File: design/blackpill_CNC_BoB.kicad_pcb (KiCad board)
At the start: 4 copper layers, 302 parts, among them J101 ALimIN, J102 ZLimIN, J103 YLimIN, J104 XLimIN, J105 CS_IN, J106 FH_IN, J107 DoorIN, J108 ResetIN, J109 ProbeIN, J110 12V Power in, J111 AuxEncIn, J112 5V Power out, J113 ADC_in_1, J114 ADC_in_2, J115 stepDriverLim, J116 Reset, J117 UART1, J118 I2C, J119 SpindleVFD, J120 Spindle/Coolant, J121 Spindle, J122 Coolant, J123 AuxOut, J124 XStepDrv, J125 YStepDrv, J126 ZStepDrv, J127 AStepDrv, J128 Driver Power in/out, J129 Relais Power in/out, U101 TLP290-4, U102 TLP290-4, U103 TLP290-4, U104 74LVC2G17, U105 LD1117S50TR_SOT223, U106 LM358, U107 TLV9001, U108 TLV9001, U109 YAAJ_WeAct_BlackPill_Part_Like, U110 TLV9001, U111 TLV9001, U112 74HCT541, U113 74HCT541, U114 74HCT541, U115 ULN2003A, U116 ULN2003A, U117 ULN2003A

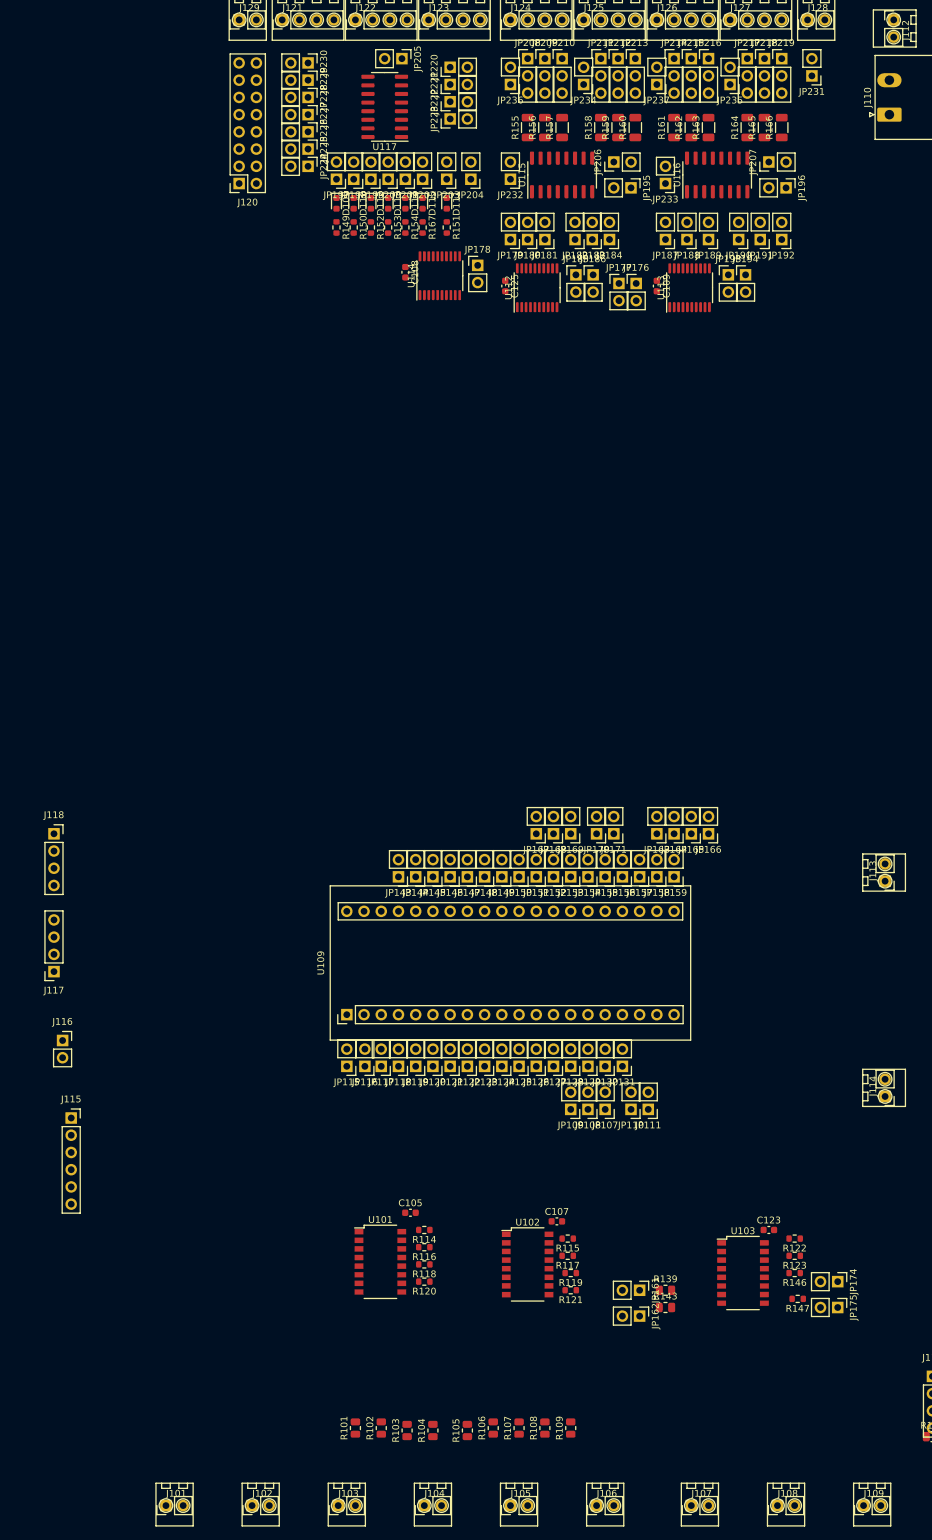
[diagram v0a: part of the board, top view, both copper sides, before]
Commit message: start placing controller
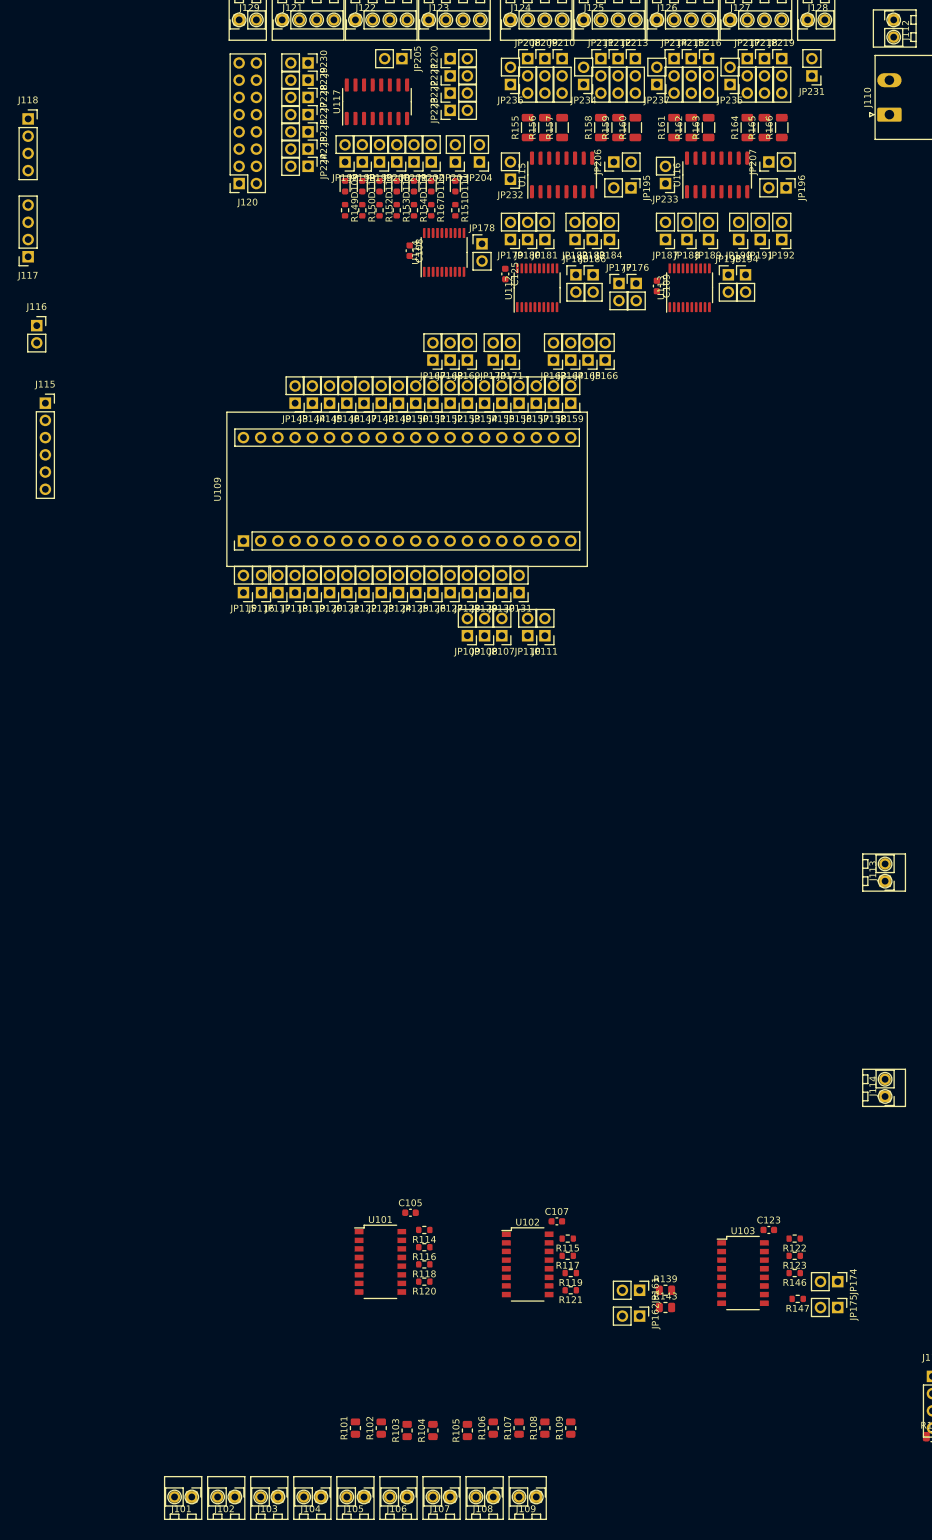
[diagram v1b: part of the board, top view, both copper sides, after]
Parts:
- moved J115 105.5 mm to (-26.7, 58.4)
- moved J117 105.5 mm to (-29.2, 36.8)
- moved J116 105.5 mm to (-27.9, 47.0)
- moved J118 105.5 mm to (-29.2, 16.5)
- moved JP107 71.5 mm to (40.6, 92.7)
- moved JP108 71.5 mm to (38.1, 92.7)
- moved JP109 71.5 mm to (35.6, 92.7)
- moved JP110 71.5 mm to (44.5, 92.7)
- moved JP111 71.5 mm to (47.0, 92.7)
- moved JP115 71.5 mm to (2.54, 86.4)
- moved JP116 71.5 mm to (5.21, 86.4)
- moved JP117 71.5 mm to (7.62, 86.4)
- moved JP118 71.5 mm to (10.2, 86.4)
- moved JP119 71.5 mm to (12.7, 86.4)
- moved JP120 71.5 mm to (15.2, 86.4)
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
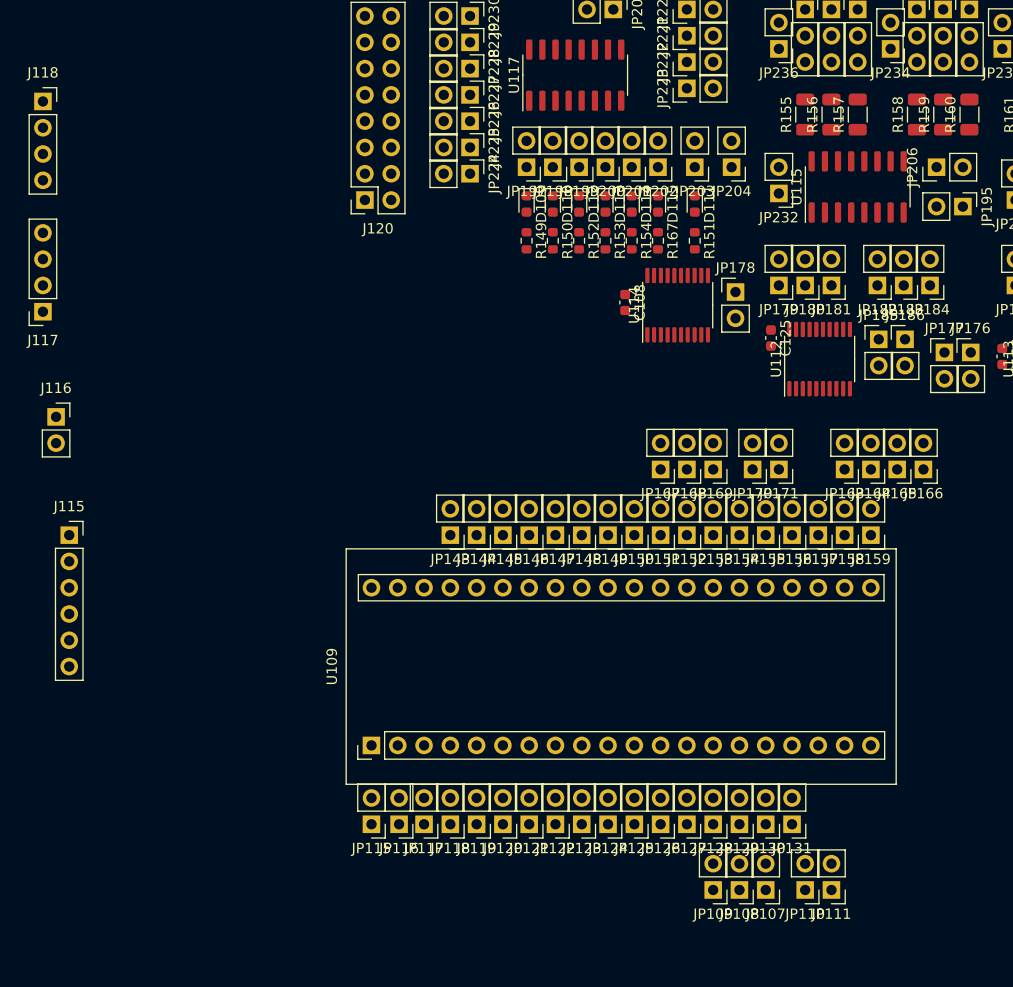
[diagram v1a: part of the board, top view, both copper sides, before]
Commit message: added exp power pins
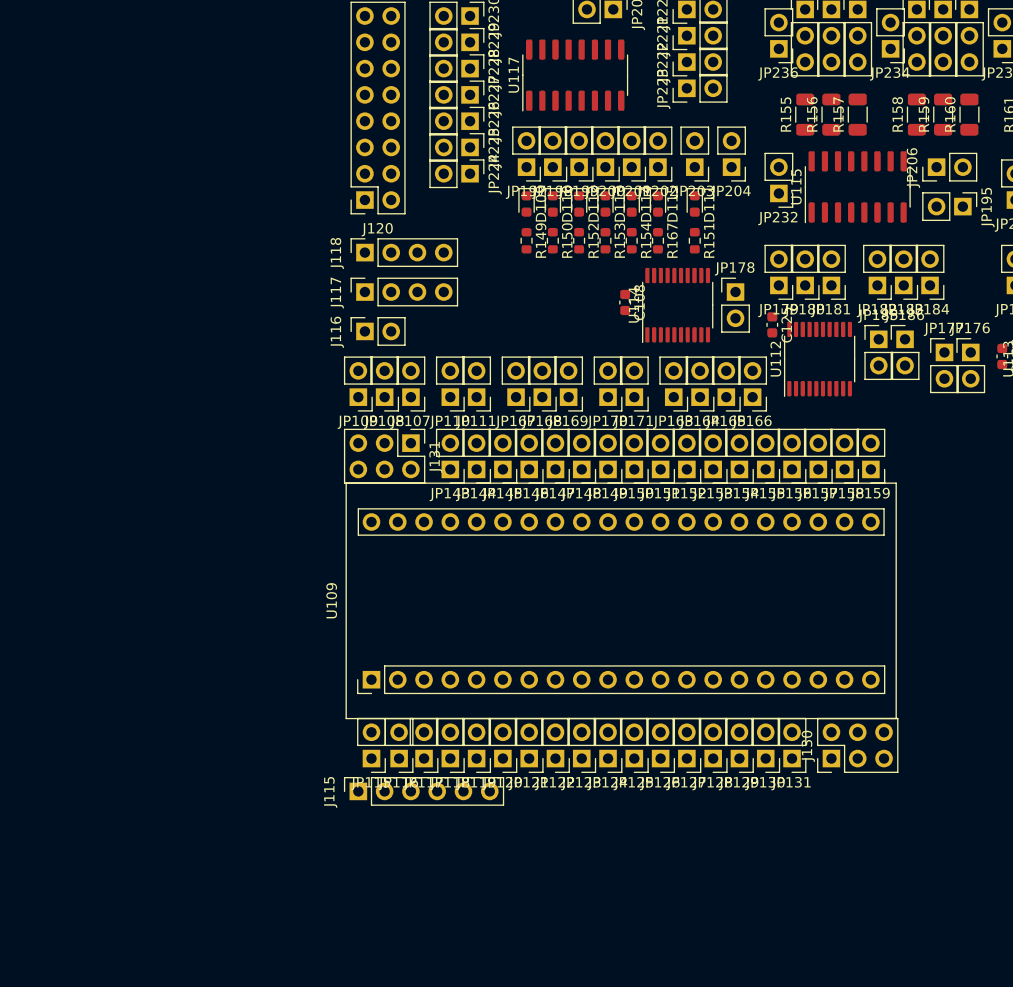
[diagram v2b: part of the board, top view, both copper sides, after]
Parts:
- added J130: Conn_02x03_Odd_Even, Connector_PinHeader_2.54mm:PinHeader_2x03_P2.54mm_Vertical, F.Cu at (47.0, 80.0)
- added J131: Conn_02x03_Odd_Even, Connector_PinHeader_2.54mm:PinHeader_2x03_P2.54mm_Vertical, F.Cu at (6.35, 49.5)
- moved JP107 58.7 mm to (6.35, 45.1)
- moved JP108 58.7 mm to (3.81, 45.1)
- moved JP109 58.7 mm to (1.27, 45.1)
- moved JP110 58.7 mm to (10.2, 45.1)
- moved JP111 58.7 mm to (12.7, 45.1)
- moved J115 37.3 mm to (1.27, 83.2), turned to 90 degrees
- moved J118 34.4 mm to (1.91, 31.1), turned to 90 degrees
- moved J117 31.2 mm to (1.91, 34.9), turned to 90 degrees
- moved J116 31.0 mm to (1.91, 38.7), turned to 90 degrees
- moved JP165 17.9 mm to (36.8, 45.1)
- moved JP166 17.9 mm to (39.4, 45.1)
- moved JP163 17.9 mm to (31.8, 45.1)
- moved JP164 17.9 mm to (34.3, 45.1)
- moved JP168 15.6 mm to (19.1, 45.1)
- moved JP169 15.6 mm to (21.6, 45.1)
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
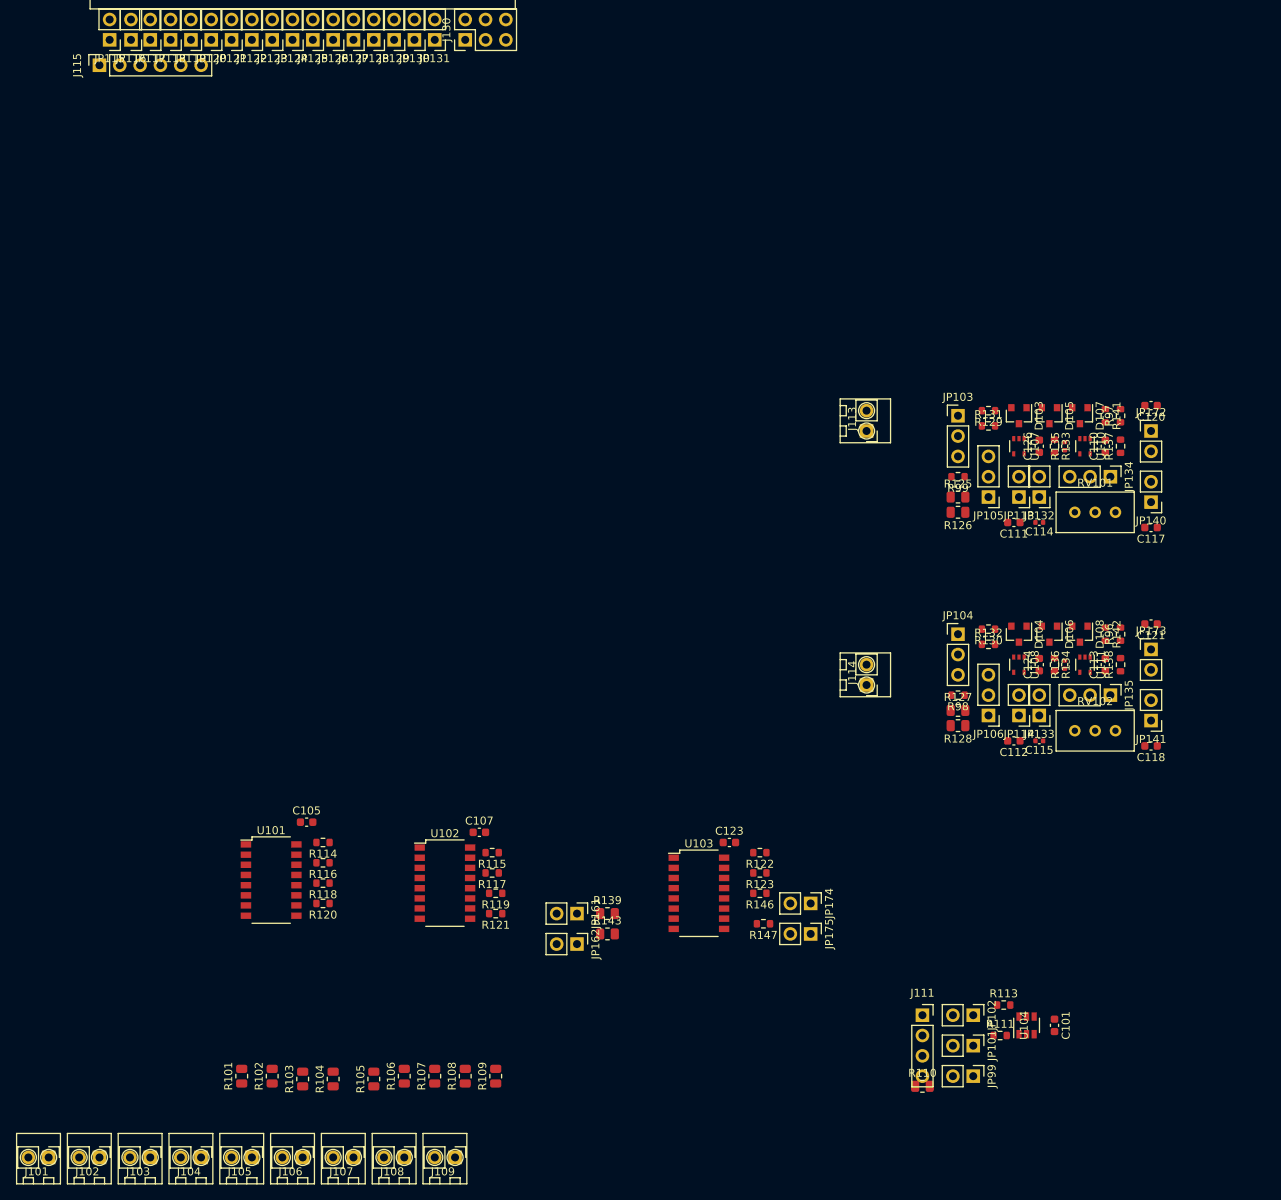
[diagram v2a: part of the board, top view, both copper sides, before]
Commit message: placed optocouplers
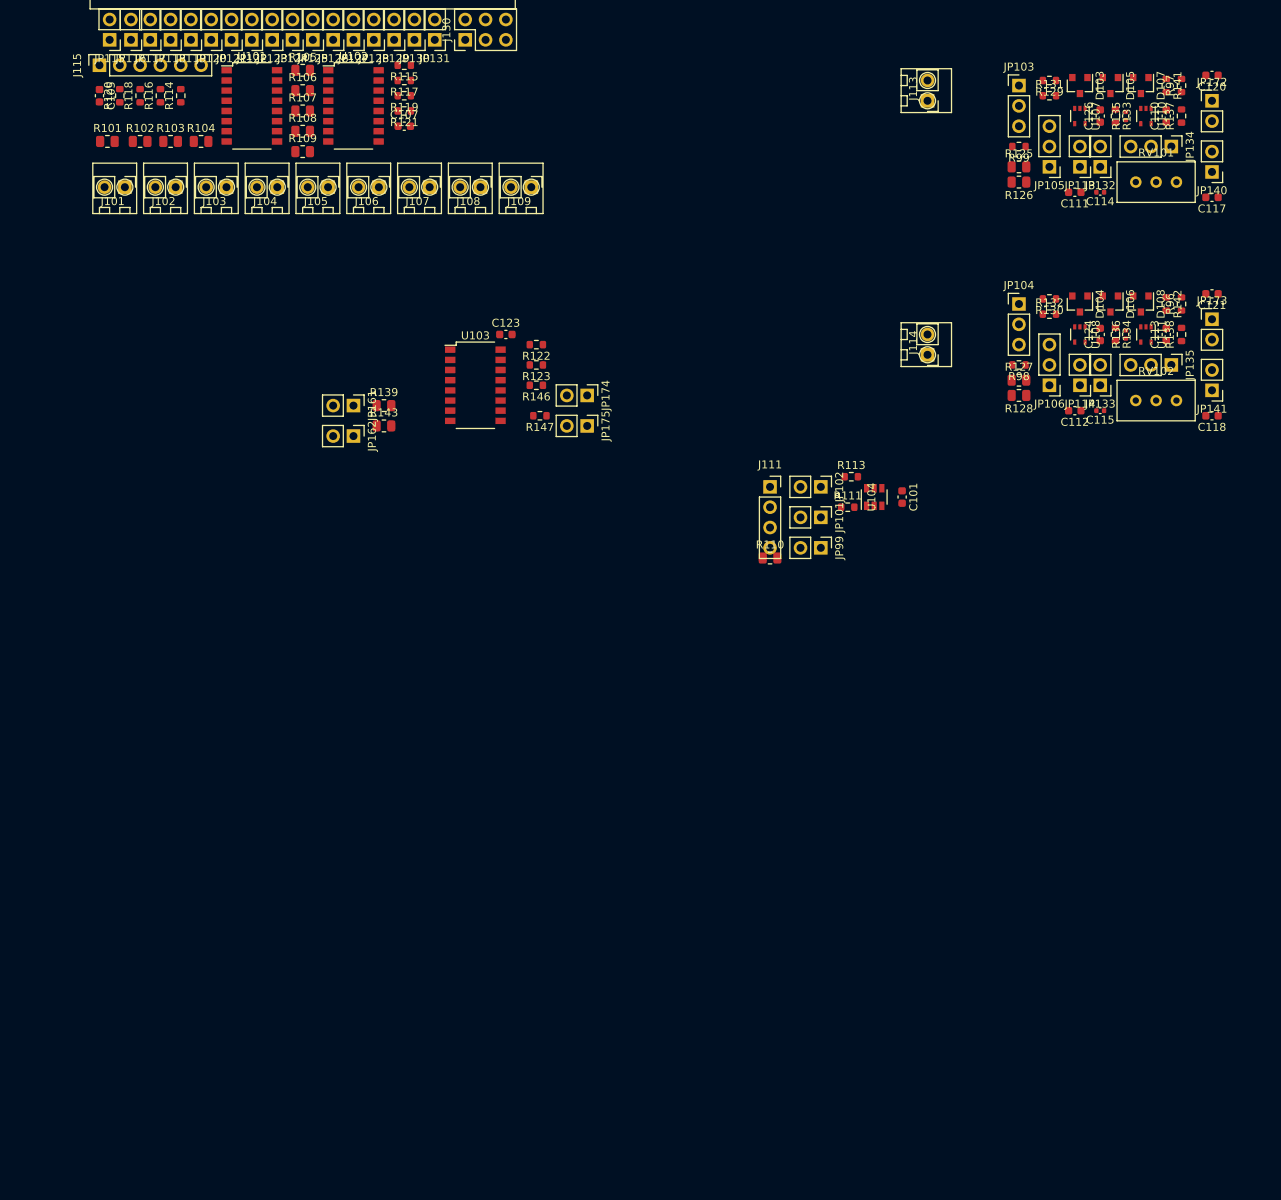
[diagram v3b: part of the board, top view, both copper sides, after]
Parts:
- moved R105 126.4 mm to (26.7, 83.8), turned to 0 degrees
- moved R106 123.8 mm to (26.7, 86.4), turned to 0 degrees
- moved R107 121.8 mm to (26.7, 88.9), turned to 0 degrees
- moved J101 121.7 mm to (4.45, 98.4)
- moved J102 121.7 mm to (10.8, 98.4)
- moved J103 121.7 mm to (17.1, 98.4)
- moved J104 121.7 mm to (23.5, 98.4)
- moved J105 121.7 mm to (29.8, 98.4)
- moved J106 121.7 mm to (36.2, 98.4)
- moved J107 121.7 mm to (42.5, 98.4)
- moved J108 121.7 mm to (48.9, 98.4)
- moved J109 121.7 mm to (55.2, 98.4)
- moved R108 119.8 mm to (26.7, 91.4), turned to 0 degrees
- moved R103 118.4 mm to (10.2, 92.7), turned to 0 degrees
- moved R104 118.4 mm to (14.0, 92.7), turned to 0 degrees
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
